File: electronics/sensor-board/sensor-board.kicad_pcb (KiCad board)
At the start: 2 copper layers, 129 parts, among them J10 Therm_1, J11 Therm_4, J12 Therm_7, J13 Therm_2, J14 Therm_5, J15 Therm_3, J16 Therm_6, J3 SWD Header, J4 Flow_1, J6 Pressure_5, J7 Pressure_6, J8 Flow_2, U1 LD3985M33R_SOT23, U10 MCP96RL01T, U11 MAX44252ASD, U12 LMC6036, U13 LMC6036, U14 LMC6036, U2 MAX33012EASA+, U3 STM32F446ZEHx, U4 MCP96RL01T, U5 MCP96RL01T, U6 MCP96RL01T, U7 MCP96RL01T, U8 MCP96RL01T, U9 MCP96RL01T

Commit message: Finalized sensor-board schematic
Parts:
- removed C1, C3: 1uF, Capacitor_SMD:C_0603_1608Metric
- removed C10, C11, C12, C13, C14, C15, C16, C17, C18, C19, C20, C21, C6, C9: 100nF, Capacitor_SMD:C_0603_1608Metric
- removed C2: 10nF, Capacitor_SMD:C_0603_1608Metric
- removed C22, C23, C24, C25, C26, C27, C28, C29, C30, C31, C32, C33, C34, C35: 0.1uF, Capacitor_SMD:C_0603_1608Metric
- removed C4, C5: 20pF, Capacitor_SMD:C_0603_1608Metric
- removed C7, C8: 2.2uF, Capacitor_SMD:C_0603_1608Metric
- removed J10: Therm_1, K_type_thermo_conn_F:K_type_thermo_conn_F
- removed J11: Therm_4, K_type_thermo_conn_F:K_type_thermo_conn_F
- removed J12: Therm_7, K_type_thermo_conn_F:K_type_thermo_conn_F
- removed J13: Therm_2, K_type_thermo_conn_F:K_type_thermo_conn_F
- removed J14: Therm_5, K_type_thermo_conn_F:K_type_thermo_conn_F
- removed J15: Therm_3, K_type_thermo_conn_F:K_type_thermo_conn_F
- removed J16: Therm_6, K_type_thermo_conn_F:K_type_thermo_conn_F
- removed J3: SWD Header, Connector_PinHeader_2.54mm:PinHeader_1x04_P2.54mm_Vertical
- removed J4: Flow_1, Connector_PinHeader_2.54mm:PinHeader_1x04_P2.54mm_Horizontal
- removed J6: Pressure_5, Connector_PinHeader_2.54mm:PinHeader_1x04_P2.54mm_Horizontal
- removed J7: Pressure_6, Connector_PinHeader_2.54mm:PinHeader_1x04_P2.54mm_Horizontal
- removed J8: Flow_2, Connector_PinHeader_2.54mm:PinHeader_1x04_P2.54mm_Horizontal
- removed R1: 0k, Resistor_SMD:R_0603_1608Metric
- removed R10, R11, R12, R13, R14, R21, R22, R23, R24, R3, R4, R5, R6, R9: 100, Resistor_SMD:R_0603_1608Metric
- removed R15, R17, R18, R2, R25, R26, R7: 10k, Resistor_SMD:R_0603_1608Metric
- removed R16: 43k, Resistor_SMD:R_0603_1608Metric
- removed R19: 2.2k, Resistor_SMD:R_0603_1608Metric
- removed R20: 13k, Resistor_SMD:R_0603_1608Metric
- removed R27: 4.3k, Resistor_SMD:R_0603_1608Metric
- removed R28: 22k, Resistor_SMD:R_0603_1608Metric
- removed R29, R30, R31, R32, R33, R34, R35, R36, R37, R38, R39, R40, R41, R42, R43, R44: R, Resistor_SMD:R_0603_1608Metric
- removed R45, R46, R47, R48, R49, R50, R51, R52, R53, R54, R55, R56, R57, R58, R59, R60, R61, R62, R63, R64, R65, R66, R67, R68: 150, Resistor_SMD:R_0603_1608Metric
- removed R8: 7.5k, Resistor_SMD:R_0603_1608Metric
- removed U1: LD3985M33R_SOT23, Package_TO_SOT_SMD:SOT-23-5
- removed U10, U4, U5, U6, U7, U8, U9: MCP96RL01T, MCP96RL01T:MCP96RL01T_QFN
- removed U11: MAX44252ASD, MAX44252ASD-:MAX44252ASD&plus_
- removed U12, U13, U14: LMC6036, LMC6036:SOP65P640X120-14N
- removed U2: MAX33012EASA+, MAX33012EASA+:MAX33012EASA+
- removed U3: STM32F446ZEHx, Package_BGA:UFBGA-144_7x7mm_Layout12x12_P0.5mm

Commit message: Schematic edit
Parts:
- added U1: STM32F446ZEH6, STM32F446ZEH6:STM32F446ZEH6, F.Cu at (139.7, 114.3)

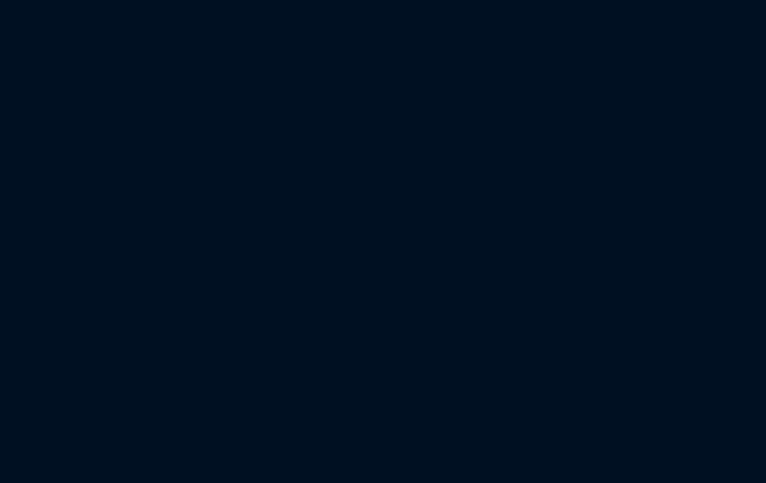
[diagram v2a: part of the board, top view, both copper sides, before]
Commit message: Added Op Amp Library to sensor-board
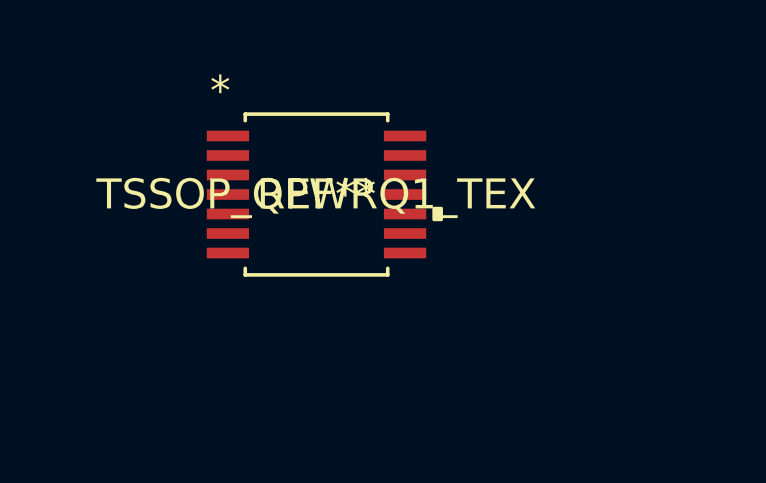
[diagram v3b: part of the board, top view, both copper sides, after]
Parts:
- added REF**: TSSOP_QPWRQ1_TEX, OPA4197QPWRQ1:OPA4197QPWRQ1, F.Cu at (127.0, 76.2)

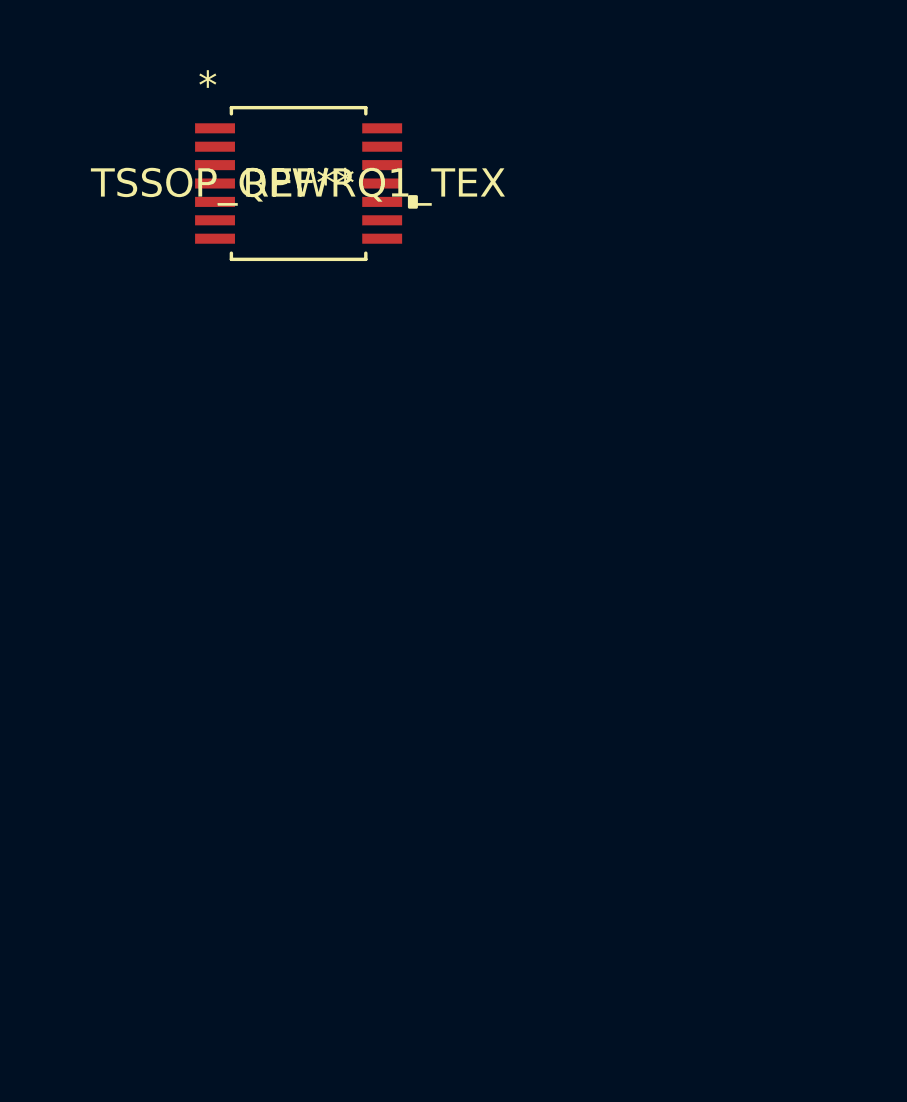
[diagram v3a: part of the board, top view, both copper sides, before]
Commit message: Switched Op Amps
Added library files for both op amps (precision and general purpose)
Couldn't find symbol library for gen-purp. op amp
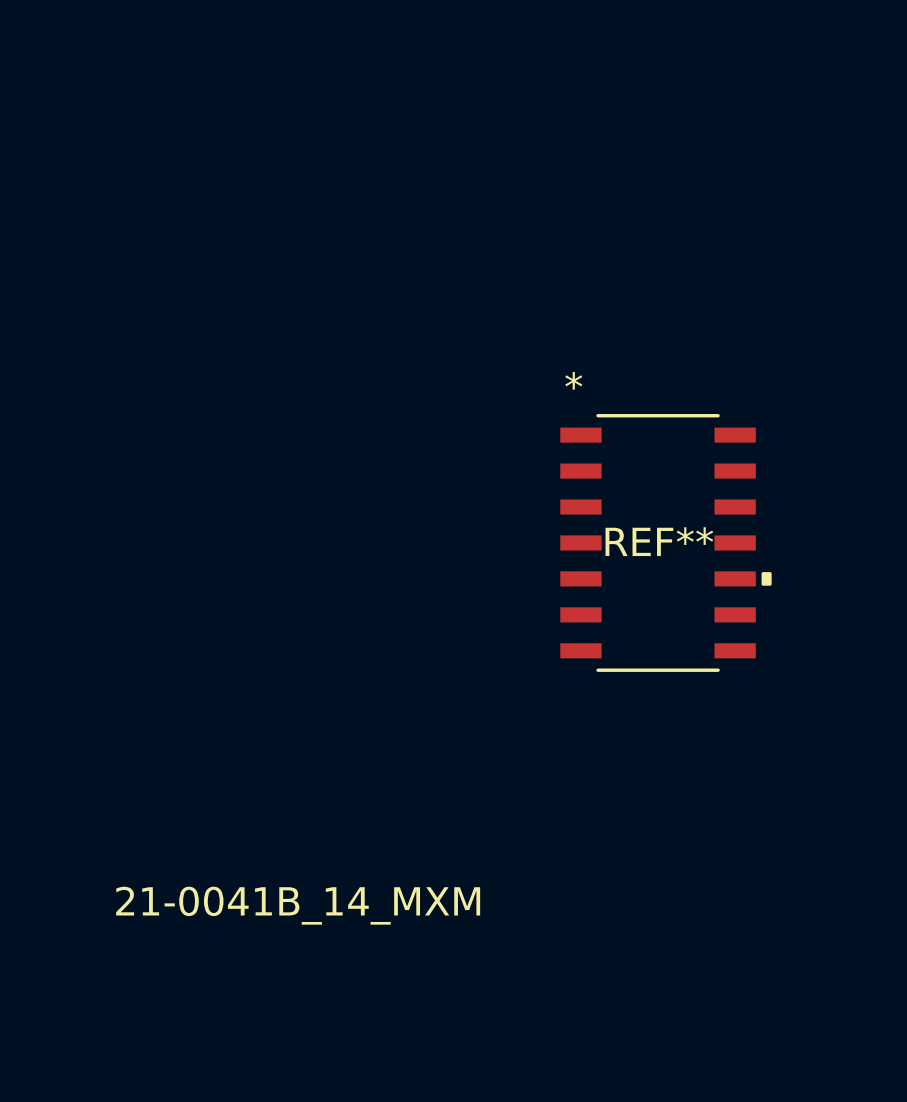
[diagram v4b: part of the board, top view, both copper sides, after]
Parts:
- removed the REF** at (127.0, 76.2)
- added REF**: 21-0041B_14_MXM, MAX44252ASD-:MAX44252ASD&plus_, F.Cu at (139.7, 88.9)

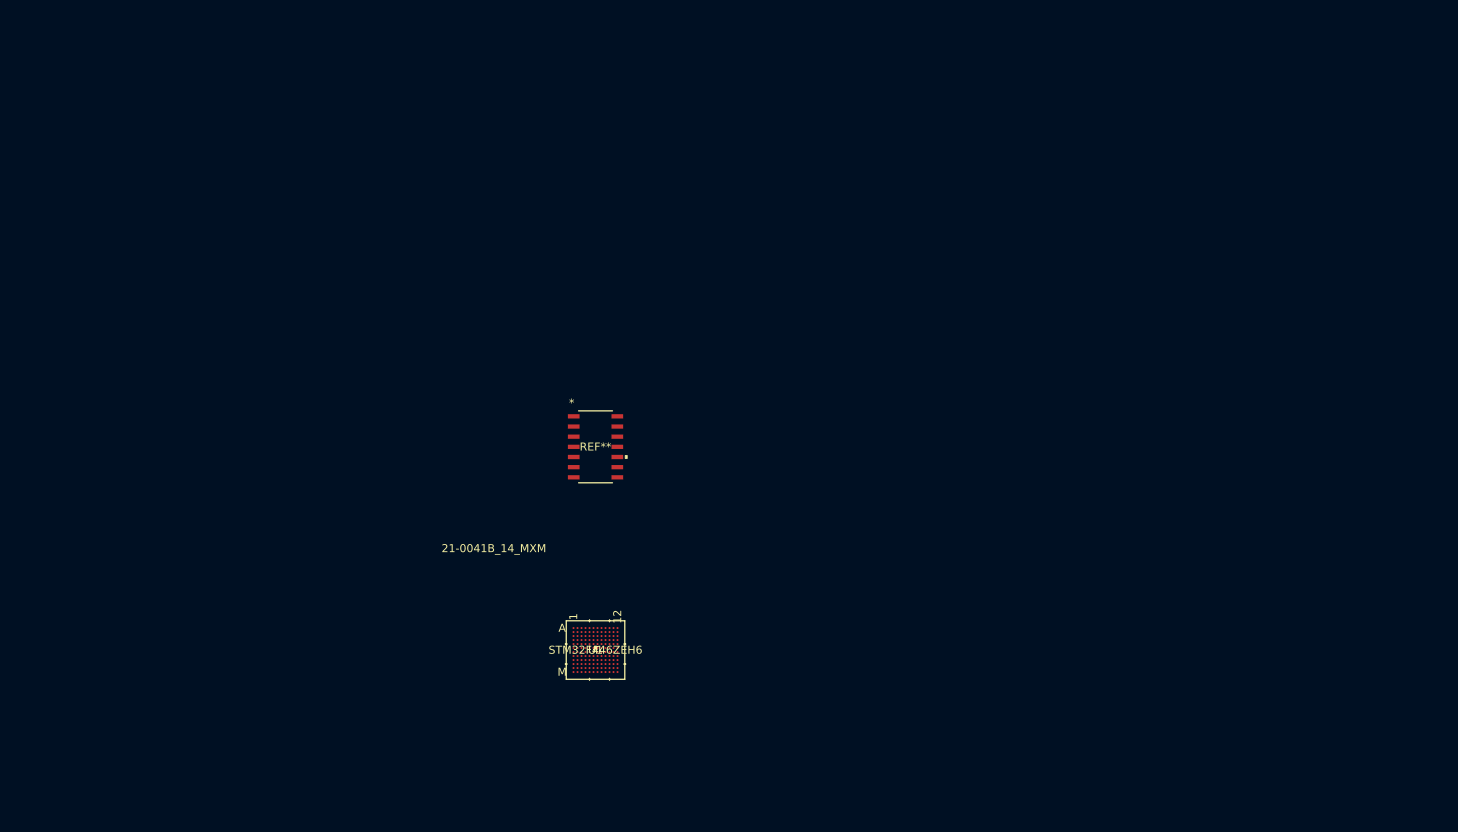
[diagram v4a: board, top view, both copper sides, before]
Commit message: work on sensor-board
thermocouple connector footprints made (selected connector)
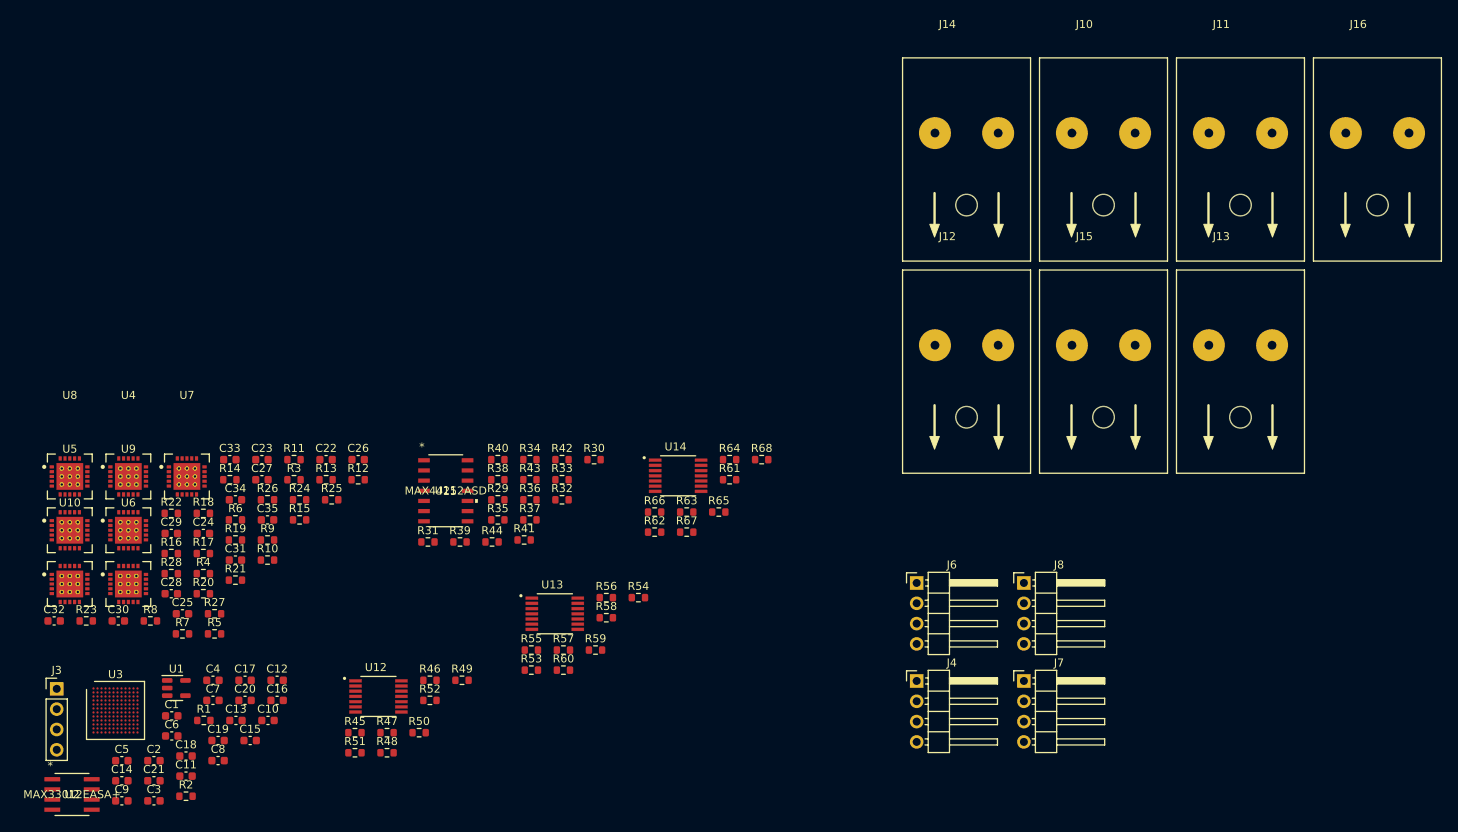
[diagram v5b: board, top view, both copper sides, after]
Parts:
- removed REF**: 21-0041B_14_MXM, MAX44252ASD-:MAX44252ASD&plus_
- added C1: 1uF, Capacitor_SMD:C_0603_1608Metric, F.Cu at (86.7, 122.5)
- added C10: 100nF, Capacitor_SMD:C_0603_1608Metric, F.Cu at (98.8, 123.1)
- added C11: 100nF, Capacitor_SMD:C_0603_1608Metric, F.Cu at (88.5, 130.1)
- added C12: 100nF, Capacitor_SMD:C_0603_1608Metric, F.Cu at (99.9, 118.1)
- added C13: 100nF, Capacitor_SMD:C_0603_1608Metric, F.Cu at (94.8, 123.1)
- added C14: 100nF, Capacitor_SMD:C_0603_1608Metric, F.Cu at (80.5, 130.6)
- added C15: 100nF, Capacitor_SMD:C_0603_1608Metric, F.Cu at (96.5, 125.6)
- added C16: 100nF, Capacitor_SMD:C_0603_1608Metric, F.Cu at (99.9, 120.6)
- added C17: 100nF, Capacitor_SMD:C_0603_1608Metric, F.Cu at (95.9, 118.1)
- added C18: 100nF, Capacitor_SMD:C_0603_1608Metric, F.Cu at (88.5, 127.5)
- added C19: 100nF, Capacitor_SMD:C_0603_1608Metric, F.Cu at (92.5, 125.6)
- added C2: 10nF, Capacitor_SMD:C_0603_1608Metric, F.Cu at (84.5, 128.1)
- added C20: 100nF, Capacitor_SMD:C_0603_1608Metric, F.Cu at (95.9, 120.6)
- added C21: 100nF, Capacitor_SMD:C_0603_1608Metric, F.Cu at (84.5, 130.6)
- added C22: 0.1uF, Capacitor_SMD:C_0603_1608Metric, F.Cu at (106.0, 90.5)
- added C23: 0.1uF, Capacitor_SMD:C_0603_1608Metric, F.Cu at (98.0, 90.5)
- added C24: 0.1uF, Capacitor_SMD:C_0603_1608Metric, F.Cu at (90.7, 99.7)
- added C25: 0.1uF, Capacitor_SMD:C_0603_1608Metric, F.Cu at (88.1, 109.8)
- added C26: 0.1uF, Capacitor_SMD:C_0603_1608Metric, F.Cu at (110.0, 90.5)
- added C27: 0.1uF, Capacitor_SMD:C_0603_1608Metric, F.Cu at (98.0, 93.0)
- added C28: 0.1uF, Capacitor_SMD:C_0603_1608Metric, F.Cu at (86.7, 107.3)
- added C29: 0.1uF, Capacitor_SMD:C_0603_1608Metric, F.Cu at (86.7, 99.7)
- added C3: 1uF, Capacitor_SMD:C_0603_1608Metric, F.Cu at (84.5, 133.2)
- added C30: 0.1uF, Capacitor_SMD:C_0603_1608Metric, F.Cu at (80.0, 110.7)
- added C31: 0.1uF, Capacitor_SMD:C_0603_1608Metric, F.Cu at (94.7, 103.0)
- added C32: 0.1uF, Capacitor_SMD:C_0603_1608Metric, F.Cu at (72.0, 110.7)
- added C33: 0.1uF, Capacitor_SMD:C_0603_1608Metric, F.Cu at (94.0, 90.5)
- added C34: 0.1uF, Capacitor_SMD:C_0603_1608Metric, F.Cu at (94.7, 95.5)
- added C35: 0.1uF, Capacitor_SMD:C_0603_1608Metric, F.Cu at (98.7, 98.0)
- added C4: 20pF, Capacitor_SMD:C_0603_1608Metric, F.Cu at (91.9, 118.1)
- added C5: 20pF, Capacitor_SMD:C_0603_1608Metric, F.Cu at (80.5, 128.1)
- added C6: 100nF, Capacitor_SMD:C_0603_1608Metric, F.Cu at (86.7, 125.0)
- added C7: 2.2uF, Capacitor_SMD:C_0603_1608Metric, F.Cu at (91.9, 120.6)
- added C8: 2.2uF, Capacitor_SMD:C_0603_1608Metric, F.Cu at (92.5, 128.1)
- added C9: 100nF, Capacitor_SMD:C_0603_1608Metric, F.Cu at (80.5, 133.2)
- added J10: Therm_1, K_type_thermo_conn_F:K_type_thermo_conn_F, F.Cu at (203.2, 49.7)
- added J11: Therm_4, K_type_thermo_conn_F:K_type_thermo_conn_F, F.Cu at (220.3, 49.7)
- added J12: Therm_7, K_type_thermo_conn_F:K_type_thermo_conn_F, F.Cu at (186.1, 76.2)
- added J13: Therm_2, K_type_thermo_conn_F:K_type_thermo_conn_F, F.Cu at (220.3, 76.2)
- added J14: Therm_5, K_type_thermo_conn_F:K_type_thermo_conn_F, F.Cu at (186.1, 49.7)
- added J15: Therm_3, K_type_thermo_conn_F:K_type_thermo_conn_F, F.Cu at (203.2, 76.2)
- added J16: Therm_6, K_type_thermo_conn_F:K_type_thermo_conn_F, F.Cu at (237.4, 49.7)
- added J3: SWD Header, Connector_PinHeader_2.54mm:PinHeader_1x04_P2.54mm_Vertical, F.Cu at (72.3, 119.2)
- added J4: Flow_1, Connector_PinHeader_2.54mm:PinHeader_1x04_P2.54mm_Horizontal, F.Cu at (179.8, 118.2)
- added J6: Pressure_5, Connector_PinHeader_2.54mm:PinHeader_1x04_P2.54mm_Horizontal, F.Cu at (179.8, 105.9)
- added J7: Pressure_6, Connector_PinHeader_2.54mm:PinHeader_1x04_P2.54mm_Horizontal, F.Cu at (193.2, 118.2)
- added J8: Flow_2, Connector_PinHeader_2.54mm:PinHeader_1x04_P2.54mm_Horizontal, F.Cu at (193.2, 105.9)
- added R1: 0k, Resistor_SMD:R_0603_1608Metric, F.Cu at (90.7, 123.1)
- added R10: 100, Resistor_SMD:R_0603_1608Metric, F.Cu at (98.7, 103.0)
- added R11: 100, Resistor_SMD:R_0603_1608Metric, F.Cu at (102.0, 90.5)
- added R12: 100, Resistor_SMD:R_0603_1608Metric, F.Cu at (110.0, 93.0)
- added R13: 100, Resistor_SMD:R_0603_1608Metric, F.Cu at (106.0, 93.0)
- added R14: 100, Resistor_SMD:R_0603_1608Metric, F.Cu at (94.0, 93.0)
- added R15: 10k, Resistor_SMD:R_0603_1608Metric, F.Cu at (102.7, 98.0)
- added R16: 43k, Resistor_SMD:R_0603_1608Metric, F.Cu at (86.7, 102.2)
- added R17: 10k, Resistor_SMD:R_0603_1608Metric, F.Cu at (90.7, 102.2)
- added R18: 10k, Resistor_SMD:R_0603_1608Metric, F.Cu at (90.7, 97.2)
- added R19: 2.2k, Resistor_SMD:R_0603_1608Metric, F.Cu at (94.7, 100.5)
- added R2: 10k, Resistor_SMD:R_0603_1608Metric, F.Cu at (88.5, 132.6)
- added R20: 13k, Resistor_SMD:R_0603_1608Metric, F.Cu at (90.7, 107.3)
- added R21: 100, Resistor_SMD:R_0603_1608Metric, F.Cu at (94.7, 105.6)
- added R22: 100, Resistor_SMD:R_0603_1608Metric, F.Cu at (86.7, 97.2)
- added R23: 100, Resistor_SMD:R_0603_1608Metric, F.Cu at (76.0, 110.7)
- added R24: 100, Resistor_SMD:R_0603_1608Metric, F.Cu at (102.7, 95.5)
- added R25: 10k, Resistor_SMD:R_0603_1608Metric, F.Cu at (106.7, 95.5)
- added R26: 10k, Resistor_SMD:R_0603_1608Metric, F.Cu at (98.7, 95.5)
- added R27: 4.3k, Resistor_SMD:R_0603_1608Metric, F.Cu at (92.1, 109.8)
- added R28: 22k, Resistor_SMD:R_0603_1608Metric, F.Cu at (86.7, 104.8)
- added R29: R, Resistor_SMD:R_0603_1608Metric, F.Cu at (127.5, 95.5)
- added R3: 100, Resistor_SMD:R_0603_1608Metric, F.Cu at (102.0, 93.0)
- added R30: R, Resistor_SMD:R_0603_1608Metric, F.Cu at (139.5, 90.5)
- added R31: R, Resistor_SMD:R_0603_1608Metric, F.Cu at (118.8, 100.8)
- added R32: R, Resistor_SMD:R_0603_1608Metric, F.Cu at (135.5, 95.5)
- added R33: R, Resistor_SMD:R_0603_1608Metric, F.Cu at (135.5, 93.0)
- added R34: R, Resistor_SMD:R_0603_1608Metric, F.Cu at (131.5, 90.5)
- added R35: R, Resistor_SMD:R_0603_1608Metric, F.Cu at (127.5, 98.0)
- added R36: R, Resistor_SMD:R_0603_1608Metric, F.Cu at (131.5, 95.5)
- added R37: R, Resistor_SMD:R_0603_1608Metric, F.Cu at (131.5, 98.0)
- added R38: R, Resistor_SMD:R_0603_1608Metric, F.Cu at (127.5, 93.0)
- added R39: R, Resistor_SMD:R_0603_1608Metric, F.Cu at (122.8, 100.8)
- added R4: 100, Resistor_SMD:R_0603_1608Metric, F.Cu at (90.7, 104.8)
- added R40: R, Resistor_SMD:R_0603_1608Metric, F.Cu at (127.5, 90.5)
- added R41: R, Resistor_SMD:R_0603_1608Metric, F.Cu at (130.8, 100.5)
- added R42: R, Resistor_SMD:R_0603_1608Metric, F.Cu at (135.5, 90.5)
- added R43: R, Resistor_SMD:R_0603_1608Metric, F.Cu at (131.5, 93.0)
- added R44: R, Resistor_SMD:R_0603_1608Metric, F.Cu at (126.8, 100.8)
- added R45: 150, Resistor_SMD:R_0603_1608Metric, F.Cu at (109.6, 124.6)
- added R46: 150, Resistor_SMD:R_0603_1608Metric, F.Cu at (119.0, 118.1)
- added R47: 150, Resistor_SMD:R_0603_1608Metric, F.Cu at (113.6, 124.6)
- added R48: 150, Resistor_SMD:R_0603_1608Metric, F.Cu at (113.6, 127.1)
- added R49: 150, Resistor_SMD:R_0603_1608Metric, F.Cu at (123.0, 118.1)
- added R5: 100, Resistor_SMD:R_0603_1608Metric, F.Cu at (92.1, 112.3)
- added R50: 150, Resistor_SMD:R_0603_1608Metric, F.Cu at (117.7, 124.6)
- added R51: 150, Resistor_SMD:R_0603_1608Metric, F.Cu at (109.6, 127.1)
- added R52: 150, Resistor_SMD:R_0603_1608Metric, F.Cu at (119.0, 120.6)
- added R53: 150, Resistor_SMD:R_0603_1608Metric, F.Cu at (131.7, 116.8)
- added R54: 150, Resistor_SMD:R_0603_1608Metric, F.Cu at (145.1, 107.8)
- added R55: 150, Resistor_SMD:R_0603_1608Metric, F.Cu at (131.7, 114.3)
- added R56: 150, Resistor_SMD:R_0603_1608Metric, F.Cu at (141.1, 107.8)
- added R57: 150, Resistor_SMD:R_0603_1608Metric, F.Cu at (135.7, 114.3)
- added R58: 150, Resistor_SMD:R_0603_1608Metric, F.Cu at (141.1, 110.3)
- added R59: 150, Resistor_SMD:R_0603_1608Metric, F.Cu at (139.7, 114.3)
- added R6: 100, Resistor_SMD:R_0603_1608Metric, F.Cu at (94.7, 98.0)
- added R60: 150, Resistor_SMD:R_0603_1608Metric, F.Cu at (135.7, 116.8)
- added R61: 150, Resistor_SMD:R_0603_1608Metric, F.Cu at (156.5, 93.0)
- added R62: 150, Resistor_SMD:R_0603_1608Metric, F.Cu at (147.1, 99.6)
- added R63: 150, Resistor_SMD:R_0603_1608Metric, F.Cu at (151.1, 97.0)
- added R64: 150, Resistor_SMD:R_0603_1608Metric, F.Cu at (156.5, 90.5)
- added R65: 150, Resistor_SMD:R_0603_1608Metric, F.Cu at (155.1, 97.0)
- added R66: 150, Resistor_SMD:R_0603_1608Metric, F.Cu at (147.1, 97.0)
- added R67: 150, Resistor_SMD:R_0603_1608Metric, F.Cu at (151.1, 99.6)
- added R68: 150, Resistor_SMD:R_0603_1608Metric, F.Cu at (160.5, 90.5)
- added R7: 10k, Resistor_SMD:R_0603_1608Metric, F.Cu at (88.1, 112.3)
- added R8: 7.5k, Resistor_SMD:R_0603_1608Metric, F.Cu at (84.1, 110.7)
- added R9: 100, Resistor_SMD:R_0603_1608Metric, F.Cu at (98.7, 100.5)
- added U10: MCP96RL01T, MCP96RL01T:MCP96RL01T_QFN, F.Cu at (74.0, 106.0)
- added U11: MAX44252ASD, MAX44252ASD-:MAX44252ASD&plus_, F.Cu at (121.0, 94.4)
- added U12: LMC6036, LMC6036:SOP65P640X120-14N, F.Cu at (112.6, 120.1)
- added U13: LMC6036, LMC6036:SOP65P640X120-14N, F.Cu at (134.6, 109.8)
- added U14: LMC6036, LMC6036:SOP65P640X120-14N, F.Cu at (150.0, 92.5)
- added U2: MAX33012EASA+, MAX33012EASA+:MAX33012EASA+, F.Cu at (74.3, 132.4)
- added U3: STM32F446ZEHx, Package_BGA:UFBGA-144_7x7mm_Layout12x12_P0.5mm, F.Cu at (79.7, 121.8)
- added U4: MCP96RL01T, MCP96RL01T:MCP96RL01T_QFN, F.Cu at (81.3, 92.6)
- added U5: MCP96RL01T, MCP96RL01T:MCP96RL01T_QFN, F.Cu at (74.0, 99.3)
- added U6: MCP96RL01T, MCP96RL01T:MCP96RL01T_QFN, F.Cu at (81.3, 106.0)
- added U7: MCP96RL01T, MCP96RL01T:MCP96RL01T_QFN, F.Cu at (88.6, 92.6)
- added U8: MCP96RL01T, MCP96RL01T:MCP96RL01T_QFN, F.Cu at (74.0, 92.6)
- added U9: MCP96RL01T, MCP96RL01T:MCP96RL01T_QFN, F.Cu at (81.3, 99.3)
- U1: value STM32F446ZEH6 -> LD3985M33R_SOT23; footprint STM32F446ZEH6:STM32F446ZEH6 -> Package_TO_SOT_SMD:SOT-23-5
- moved U1 52.6 mm to (87.3, 119.0)
